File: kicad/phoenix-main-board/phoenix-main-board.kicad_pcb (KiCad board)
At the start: 2 copper layers, 50.8 x 22.9 mm, 87 parts, among them U1 LT3092xDD, U2 LM7705, U3 Adafruit_Feather_nrf52840_Exp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, U4 MCP3564, U5 TS5A3359, U6 TPS61222DCK, U7 OPA2380, U8 TPS7A2033DQN, U9 AD5242

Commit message: finish majority of pcb design
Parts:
- removed C10, C11: 100nF, Capacitor_SMD:C_0603_1608Metric
- removed JP5: SolderJumper_2_Bridged, Jumper:SolderJumper-2_P1.3mm_Bridged_RoundedPad1.0x1.5mm
- removed JP6: SolderJumper_2_Open, Jumper:SolderJumper-2_P1.3mm_Open_RoundedPad1.0x1.5mm
- removed R13, R14: 100, Resistor_SMD:R_0603_1608Metric
- removed TP35: TestPoint_Small, TestPoint:TestPoint_Keystone_5000-5004_Miniature
- added G***: LOGO, LOGO, B.Cu at (96.5, 50.7)
- added JP1: SolderJumper_3_Bridged12, Jumper:SolderJumper-3_P1.3mm_Bridged2Bar12_Pad1.0x1.5mm, F.Cu at (64.5, 42.0)
- added R23: 10k, Resistor_SMD:R_0603_1608Metric, F.Cu at (112.0, 68.9)
- added R24: 10k, Resistor_SMD:R_0603_1608Metric, F.Cu at (113.5, 68.9)
- added REF**: MountingHole_3.2mm_M3, MountingHole:MountingHole_3.2mm_M3, F.Cu at (33.5, 23.5)
- added REF**: MountingHole_3.2mm_M3, MountingHole:MountingHole_3.2mm_M3, F.Cu at (135.0, 74.5)
- added REF**: MountingHole_3.2mm_M3, MountingHole:MountingHole_3.2mm_M3, F.Cu at (135.0, 23.5)
- added REF**: MountingHole_3.2mm_M3, MountingHole:MountingHole_3.2mm_M3, F.Cu at (33.5, 74.5)
- added TP27: TestPoint_Small, TestPoint:TestPoint_Keystone_5000-5004_Miniature, F.Cu at (128.5, 71.0)
- added TP37: TestPoint_Small, TestPoint:TestPoint_Keystone_5000-5004_Miniature, F.Cu at (86.0, 58.9)
- added TP5: TestPoint_Small, TestPoint:TestPoint_Keystone_5000-5004_Miniature, F.Cu at (108.6, 65.3)
- D1, D2, PD1, PD2: footprint LED_THT:LED_D5.0mm -> LED_THT:LED_D5.0mm_Horizontal_O1.27mm_Z3.0mm
- TH2: footprint Connector_Wire:SolderWire-0.1sqmm_1x02_P3.6mm_D0.4mm_OD1mm_Relief -> Resistor_SMD:R_0603_1608Metric
- U3: moved to B.Cu
- moved TP36 208.4 mm to (36.1, 47.2)
- moved TP24 200.0 mm to (35.9, 42.5)
- moved TP33 180.9 mm to (63.9, 25.2)
- moved TP32 180.7 mm to (63.8, 28.9)
- moved TP25 178.2 mm to (63.5, 49.5)
- moved TP26 177.4 mm to (63.4, 46.2)
- moved TP9 165.3 mm to (63.1, 55.3)
- moved TP10 161.7 mm to (65.5, 34.6)
- moved TP11 160.2 mm to (67.0, 50.4)
- moved TP34 153.6 mm to (94.0, 70.1)
- moved TP14 147.6 mm to (86.0, 55.5)
- moved TP13 145.1 mm to (89.0, 53.7)
- moved TP15 144.2 mm to (89.0, 57.2)
- moved TP12 141.2 mm to (86.0, 52.0)
- moved C21 126.9 mm to (69.5, 28.3), turned to -90 degrees
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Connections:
- C12 pad 1: /CH2 -> /CH4
- C12 pad 2: GNDA -> GND
- C13 pad 1: /CH3 -> /CH5
- C13 pad 2: GNDA -> GND
- C4 pad 2: GNDA -> GND
- C5 pad 2: GNDA -> GND
- C6 pad 2: GNDA -> GND
- R15 pad 1: /CH2 -> /CH4
- R15 pad 2: /THERM1_SIG -> /PD1_SIG
- R16 pad 1: /CH3 -> /CH5
- R16 pad 2: /THERM2_SIG -> /PD2_SIG
- R21 pad 1: /Thermistor1 -> /Thermistor_On
- R21 pad 2: /THERM1_SIG -> /CH1
- R22 pad 1: /Thermistor2 -> /Thermistor_On
- R22 pad 2: /THERM2_SIG -> /CH2
- TH1 pad 1: /THERM2_SIG -> /CH2
- TH2 pad 1: /THERM1_SIG -> /CH1
- TP3 pad 1: /CH2 -> /CH4
- TP34 pad 1: /Thermistor1 -> /Thermistor_On
- TP4 pad 1: /CH3 -> /CH5
- U3 pad 22: /Thermistor1 -> /Thermistor_On
- U3 pad 23: /Thermistor2 -> unconnected-(U3-10_(D10)-Pad23)
- U3 pad 25: /IN1 -> unconnected-(U3-6_(D6)-Pad25)
- U3 pad 26: /IN2 -> unconnected-(U3-5_(D5)-Pad26)
- U3 pad 7: /MCLK -> unconnected-(U3-16_(A2)-Pad7)
- U4 pad 2: GNDA -> GND
- U4 pad 3: GNDA -> GND
- U7 pad 5: +3.3V -> +3.3VA
- U9 pad 5: +3.3V -> +3.3VA
- U9 pad 6: /EnablePower -> +3.3VA
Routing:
- net GND: track 0.00 -> 314.5 mm, vias 0 -> 161
- net /SDA: track 0.00 -> 144.0 mm, vias 0 -> 2
- net /SCL: track 0.00 -> 140.9 mm, vias 0 -> 1
- net +3.3V: track 6.64 -> 114.6 mm
- net +5V: track 10.0 -> 93.2 mm, vias 0 -> 3
- net /Thermistor_On: track 0.00 -> 80.4 mm
- net /~{MCP_CS}: track 0.00 -> 78.3 mm, vias 0 -> 2
- net /~{IRQ}: track 5.56 -> 81.2 mm, vias 0 -> 1
- net /EnablePower: track 0.00 -> 71.8 mm, vias 0 -> 3
- net -0.23V: track 5.19 -> 64.9 mm
- net /MISO: track 0.00 -> 57.5 mm
- net /MOSI: track 0.00 -> 57.3 mm
- net /SCK: track 0.00 -> 57.2 mm
- net +3.3VA: track 1.89 -> 47.7 mm, vias 0 -> 2
- net /IN2: track 0.00 -> 25.0 mm, vias 0 -> 1
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- added copper zone on In1.Cu, net GND
- added copper zone on In2.Cu, net GND
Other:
- board size 50.8 x 22.9 mm -> 108.8 x 58 mm
- copper layers 2 -> 4
- board text added: "Phoenix Pro V1.0.0 - {dblquote}Stormcloud{dblquote} 2025-07-17 Phalkon Industries Jonathan Pfeifer"

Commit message: v1.0.0 release
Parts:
- added ?: , , F.Cu at (135.0, 58.0)
- added ?: , , F.Cu at (38.5, 75.0)
- added REF**: Fiducial_1mm_Mask2mm, Fiducial:Fiducial_1mm_Mask2mm, F.Cu at (40.0, 23.5)
- REF** (x4): value MountingHole_3.2mm_M3 -> MountingHole_3.2mm_M3_DIN965_Pad_TopBottom; footprint MountingHole:MountingHole_3.2mm_M3 -> MountingHole:MountingHole_3.2mm_M3_DIN965_Pad_TopBottom
- moved REF** 0.50 mm to (134.5, 74.5)
- moved REF** 0.50 mm to (134.5, 23.5)
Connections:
- net Net-(D1-A) renamed /CSOURCE
- net Net-(D1-K) renamed /NO0
- net Net-(D2-K) renamed /NO1
- net Net-(U5-NO2) renamed /NO2
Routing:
- net /~{IRQ}: track 81.2 -> 80.3 mm
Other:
- board size 108.8 x 58 mm -> 108 x 58 mm
- board text added: "-0.23V"
- board text added: "3.3V"
- board text added: "3.3VA"
- board text added: "5V"
- board text added: "CH0"
- board text added: "CH1"
- board text added: "CH2"
- board text added: "CH4"
- board text added: "CH5"
- board text added: "CSOURCE"
- board text added: "ENPWR"
- board text added: "GND"
- board text added: "IN1"
- board text added: "IN2"
- board text added: "MISO"
- board text added: "MOSI"
- board text added: "NO0"
- board text added: "NO1"
- board text added: "NO2"
- board text added: "Phoenix V1.0.0 - {dblquote}Stormcloud{dblquote} 2025-07-17 Phalkon Industries Jonathan Pfeifer"
- board text added: "SCK"
- board text added: "SCL"
- board text added: "SDA"
- board text added: "THERMON"
- board text added: "VBAT"
- board text added: "VBUS"
- board text added: "~{IRQ}"
- board text added: "~{MCP_CS}"
- board text removed: "Phoenix Pro V1.0.0 - {dblquote}Stormcloud{dblquote} 2025-07-17 Phalkon Industries Jonathan Pfeifer"

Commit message: Work on pick n place files
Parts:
- gave numbers to parts that had none: 2
- renumbered REF** to FID1
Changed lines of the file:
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@@
 		(allow_soldermask_bridges_in_footprints no)
 		(tenting front back)
+		(aux_axis_origin 33.5 74.5)
 		(grid_origin 30 20)
 		(pcbplotparams
@@
 			(drillshape 0)
 			(scaleselection 1)
-			(outputdirectory "")
+			(outputdirectory "./output")
 		)
 	)
@@
 		(layer "F.Cu")
 		(at 135 58)
-		(property "Reference" ""
+		(property "Reference" "FID3"
 			(at 1.5 -1 0)
 			(layer "F.SilkS")
+			(hide yes)
 			(effects
 				(font
@@
 		(layer "F.Cu")
 		(at 38.5 75)
-		(property "Reference" ""
+		(property "Reference" "FID2"
 			(at 1.5 -1 0)
 			(layer "F.SilkS")
+			(hide yes)
 			(effects
 				(font
@@
 		(descr "Circular Fiducial, 1mm bare copper, 2mm soldermask opening (Level A)")
 		(tags "fiducial")
-		(property "Reference" "REF**"
+		(property "Reference" "FID1"
 			(at 0 -2 0)
 			(layer "F.SilkS")

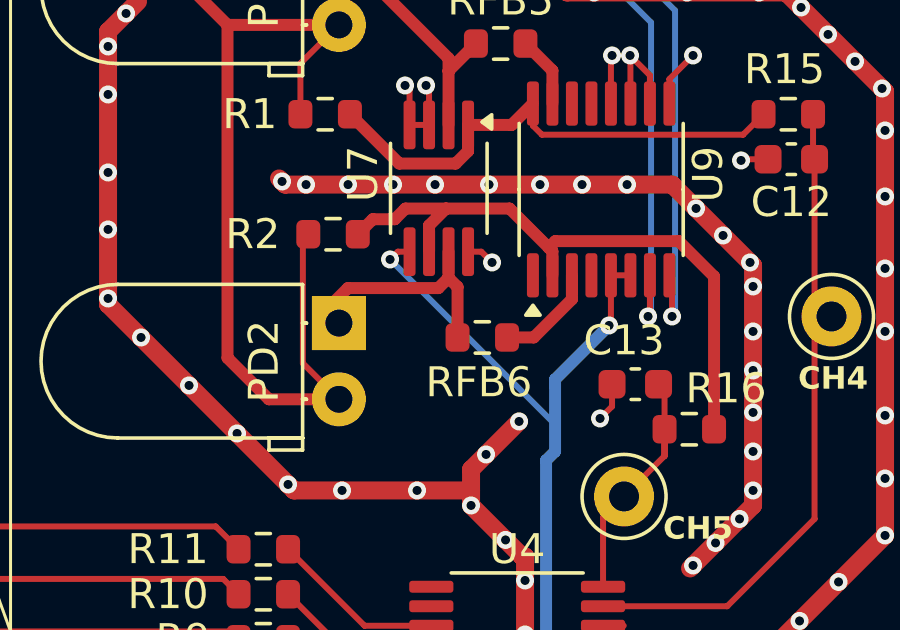
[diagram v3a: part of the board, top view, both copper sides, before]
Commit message: PCB: Fix OPA2380 pinout
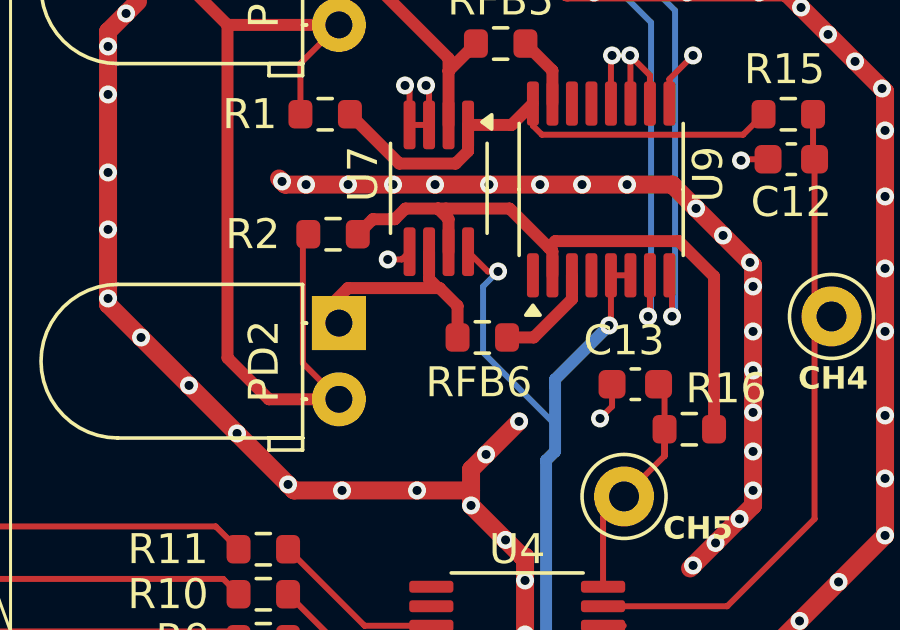
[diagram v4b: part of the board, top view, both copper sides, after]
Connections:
- U7 pad 5: +3.3VA -> GND
- U7 pad 6: /PD2_SIG -> Net-(PD2-K)
- U7 pad 7: Net-(PD2-K) -> /PD2_SIG
- U7 pad 8: GND -> +3.3VA
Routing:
- net +3.3VA: track 47.7 -> 46.7 mm

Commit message: PCB: Fix LM7705 SD wrong polarity
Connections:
- U2 pad 3: /EnablePower -> GND
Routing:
- net /EnablePower: track 71.8 -> 52.8 mm, vias 3 -> 1
- net GND: track 314.4 -> 315.1 mm
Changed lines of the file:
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@@
 			(layers "F.Cu" "F.Mask" "F.Paste")
 			(roundrect_rratio 0.25)
-			(net 36 "/EnablePower")
+			(net 3 "GND")
 			(pinfunction "SD")
 			(pintype "input")
@@
 	)
 	(segment
+		(start 72.975 26.1)
+		(end 72.975 26.75)
+		(width 0.2)
+		(layer "F.Cu")
+		(net 3)
+	)
+	(segment
 		(start 136.4 52.3)
 		(end 134.85 53.85)
@@
 	)
 	(segment
-		(start 74.0885 27.095082)
-		(end 74.0885 29.4115)
-		(width 0.2)
-		(layer "F.Cu")
-		(net 36)
-	)
-	(segment
 		(start 66.9 50.3)
 		(end 66.9 46.9)
@@
 	)
 	(segment
-		(start 72.975 26.75)
-		(end 73.743418 26.75)
-		(width 0.2)
-		(layer "F.Cu")
-		(net 36)
-	)
-	(segment
-		(start 73.743418 26.75)
-		(end 74.0885 27.095082)
-		(width 0.2)
-		(layer "F.Cu")
-		(net 36)
-	)
-	(segment
-		(start 66.9 36.6)
-		(end 66.3 37.2)
-		(width 0.2)
-		(layer "F.Cu")
-		(net 36)
-	)
-	(segment
 		(start 52.69 37.91)
 		(end 40.9 49.7)
@@
 	)
 	(segment
-		(start 66.3 37.2)
-		(end 64.1 37.2)
-		(width 0.2)
-		(layer "F.Cu")
-		(net 36)
-	)
-	(segment
 		(start 68.1505 51.5505)
 		(end 68.1505 59.0255)
@@
 	)
 	(segment
-		(start 74.0885 29.4115)
-		(end 66.9 36.6)
-		(width 0.2)
-		(layer "F.Cu")
-		(net 36)
-	)
-	(segment
 		(start 64.048 44.7)
 		(end 62.4 43.052)
@@
 	)
 	(via
-		(at 62.4 38.3)
-		(size 0.6)
-		(drill 0.3)
-		(layers "F.Cu" "B.Cu")
-		(net 36)
-	)
-	(via
-		(at 64.1 37.2)
-		(size 0.6)
-		(drill 0.3)
-		(layers "F.Cu" "B.Cu")
-		(net 36)
-	)
-	(via
 		(at 40.9 49.7)
 		(size 0.6)
@@
 		(width 0.2)
 		(layer "B.Cu")
-		(net 36)
-	)
-	(segment
-		(start 63.5 37.2)
-		(end 62.4 38.3)
-		(width 0.2)
-		(layer "B.Cu")
-		(net 36)
-	)
-	(segment
-		(start 64.1 37.2)
-		(end 63.5 37.2)
-		(width 0.2)
-		(layer "B.Cu")

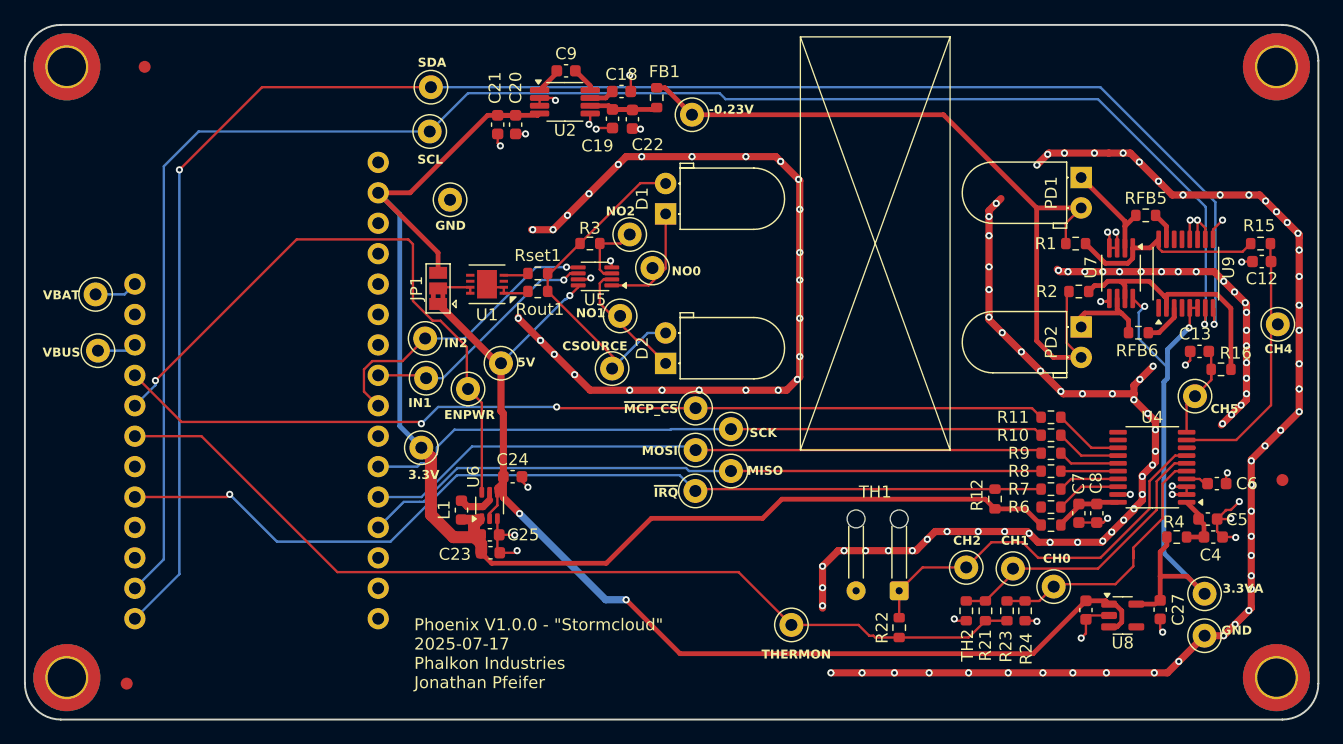
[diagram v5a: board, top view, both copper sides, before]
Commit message: PCB: Update to V1.0.1. Begin preparation for production
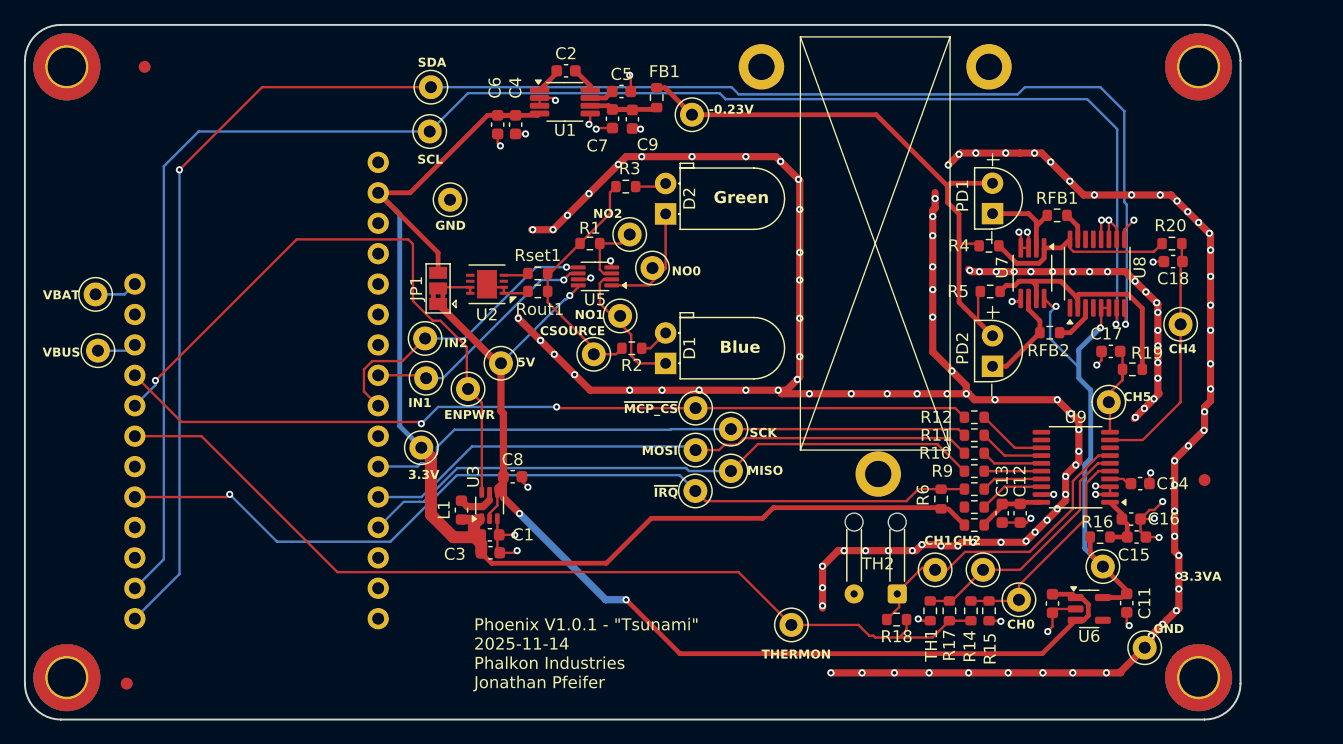
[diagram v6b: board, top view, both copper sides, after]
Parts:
- removed G***: LOGO, LOGO
- added R2: 0, Resistor_SMD:R_0603_1608Metric, F.Cu at (80.7, 47.0)
- added R3: 75, Resistor_SMD:R_0603_1608Metric, F.Cu at (80.2, 33.5)
- added REF**: MountingHole_2.2mm_M2_DIN965_Pad, MountingHole:MountingHole_2.2mm_M2_DIN965_Pad, F.Cu at (101.2, 57.5)
- added REF**: MountingHole_2.2mm_M2_DIN965_Pad, MountingHole:MountingHole_2.2mm_M2_DIN965_Pad, F.Cu at (110.5, 23.5)
- added REF**: MountingHole_2.2mm_M2_DIN965_Pad, MountingHole:MountingHole_2.2mm_M2_DIN965_Pad, F.Cu at (91.5, 23.5)
- PD1, PD2: footprint LED_THT:LED_D5.0mm_Horizontal_O1.27mm_Z3.0mm -> -ProjectLibrary:PD_Vertical
- R1: renamed from R3; value 175 -> 182
- moved TP23 8.79 mm to (120.0, 65.2)
- moved TP27 8.11 mm to (126.5, 45.0)
- moved PD2 8.09 mm to (110.8, 48.5), turned to 90 degrees
- moved PD1 7.99 mm to (110.8, 35.8), turned to 90 degrees
- moved C18 7.40 mm to (125.9, 39.8)
- moved R19 7.40 mm to (122.5, 48.8)
- moved R20 7.40 mm to (125.8, 38.3)
- moved R5 7.40 mm to (110.6, 42.3)
- moved RFB1 7.40 mm to (116.2, 35.9)
- moved U7 7.40 mm to (114.1, 40.7)
- moved U8 7.40 mm to (119.5, 40.8)
- moved C17 7.40 mm to (120.7, 47.3)
- moved RFB2 7.40 mm to (115.6, 45.7)
- moved R4 7.24 mm to (110.5, 38.4)
- moved TP28 7.22 mm to (120.5, 51.5)
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- renumbered C25 to C1, C26 to C10, C27 to C11, C8 to C12, C7 to C13, C6 to C14, C4 to C15, C5 to C16, C13 to C17, C12 to C18, C9 to C2, C23 to C3, C20 to C4, C18 to C5, C21 to C6, C19 to C7, C24 to C8, C22 to C9, D2 to D1, D1 to D2, R9 to R10, R10 to R11, R11 to R12, R5 to R13, R23 to R14, R24 to R15, R4 to R16, R21 to R17, R22 to R18, R16 to R19, R15 to R20, R1 to R4, R2 to R5, R12 to R6, R6 to R7, R7 to R8, R8 to R9, RFB5 to RFB1, RFB6 to RFB2, TH2 to TH1, TH1 to TH2, TP9 to TP1, TP19 to TP10, TP31 to TP11, TP17 to TP12, TP24 to TP13, TP36 to TP14, TP16 to TP15, TP32 to TP16, TP33 to TP17, TP37 to TP18, TP12 to TP19, TP10 to TP2, TP34 to TP20, TP11 to TP21, TP27 to TP22, TP1 to TP24, TP2 to TP25, TP5 to TP26, TP3 to TP27, TP4 to TP28, TP13 to TP3, TP14 to TP4, TP15 to TP5, TP25 to TP6, TP26 to TP7, TP20 to TP8, TP18 to TP9, U2 to U1, U1 to U2, U6 to U3, U3 to U4, U8 to U6, U9 to U8, U4 to U9
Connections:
- D1 pad 2: /CSOURCE -> Net-(D1-A)
- D2 pad 2: /CSOURCE -> Net-(D2-A)
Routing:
- net -0.23V: track 64.9 -> 51.9 mm
- net /CSOURCE: track 29.2 -> 21.1 mm
- net /CH2: track 33.4 -> 25.5 mm
- net +3.3V: track 114.6 -> 107.0 mm
- net /SCK: track 57.2 -> 50.8 mm
- net /~{MCP_CS}: track 78.3 -> 71.9 mm
- net +3.3VA: track 46.7 -> 40.3 mm
- net /MOSI: track 57.3 -> 51.8 mm
- net /~{IRQ}: track 80.3 -> 74.8 mm
- net /MISO: track 57.5 -> 53.0 mm
- net /SCL: track 140.9 -> 137.4 mm
- net /CH0: track 21.9 -> 18.5 mm
- net /CH1: track 24.1 -> 21.2 mm
- net Net-(D2-A): track 0.00 -> 2.61 mm
- net /SDA: track 144.0 -> 141.4 mm
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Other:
- board size 108 x 58 mm -> 101.5 x 58 mm
- board text added: "Blue"
- board text added: "Green"
- board text added: "Phoenix V1.0.1 - {dblquote}Tsunami{dblquote} 2025-11-14 Phalkon Industries Jonathan Pfeifer"
- board text removed: "Phoenix V1.0.0 - {dblquote}Stormcloud{dblquote} 2025-07-17 Phalkon Industries Jonathan Pfeifer"

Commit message: PCB: Complete V1.0.1 Tsunami
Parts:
- added G***: LOGO, LOGO, F.Cu at (49.5, 49.5)
- added G***: LOGO, LOGO, B.Cu at (97.0, 49.0)
- added TP29: TestPoint_Small, TestPoint:TestPoint_Keystone_5000-5004_Miniature, F.Cu at (36.0, 57.0)
- R2: value 0 -> 5
- moved TP28 1.00 mm to (121.5, 51.5)
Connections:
- U1 pad 3: GND -> /LM7705_SD
- U4 pad 23: unconnected-(U4-10_(D10)-Pad23) -> /LM7705_SD
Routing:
- net /LM7705_SD: track 0.00 -> 62.4 mm, vias 0 -> 2
- net GND: track 314.7 -> 313.7 mm
- net /NO2: track 6.12 -> 7.05 mm
- net /NO0: track 9.67 -> 9.01 mm
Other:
- board text added: "Phoenix V1.0.1 - {dblquote}Tsunami{dblquote} 2025-11-24 Phalkon Industries Jonathan Pfeifer"
- board text added: "SD"
- board text removed: "Phoenix V1.0.1 - {dblquote}Tsunami{dblquote} 2025-11-14 Phalkon Industries Jonathan Pfeifer"
